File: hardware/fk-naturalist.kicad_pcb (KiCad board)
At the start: 2 copper layers, 28.7 x 87.4 mm, 132 parts, among them J1 CONN_01X06, J10 S2B-PH-SM4-TB, J11 RF-SMA-EDGE, J5 Conn_01x03, J6 Conn_01x05, J7 CONN-HDR-2x5, J8 Conn_01x09, J9 MICRO-USB, M1 MOUNT_HOLE, M3 MOUNT_HOLE, M4 MOUNT_HOLE, M6 MOUNT_HOLE, M7 MICROSD, Q1 2N7002LT1G, Q2 2N7002LT1G, Q3 2N7002LT1G, Q4 2N7002LT1G, SW1 SPNO, SW2 SPNO, U1 ATWINC1500-MR210PA, U10 FGPMMOPA6H, U101 TSL2591, U102 MPL3115A2, U103 BNO055, U104 SHT31, U11 MAX1704XX, U2 ATSAMD21G18A-AU, U3 SPH0645, U4 24AA02E64, U5 S25FL116K0XMFI041, U6 BQ24074RGTT, U7 PCF8523, U8 MCP1700T-3302E/MB, U9 ISL8541x, Y1 FC-135, Y101 FC-135, Y2 FC-135

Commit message: Working on the new PCB layout.
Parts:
- removed C2: 100nF, RocketScreamKicadLibrary:CAP-0603
- removed C23: 1uF 10V X5R, RocketScreamKicadLibrary:CAP-0603
- removed J1: CONN_01X06, Socket_Strips:Socket_Strip_Straight_1x06_Pitch2.54mm
- removed R101: 10K, Resistors_SMD:R_0603_HandSoldering
- removed U8: MCP1700T-3302E/MB, RocketScreamKicadLibrary:SOT-89
- BT1: footprint Connectors:CR1220 -> conservify:BAT_CR1210; moved to B.Cu
- C1: value 4.7uF 10V X5R -> 1uF
- C101, C102, C103, C104, C105, C106, C107, C108, C109, C13, C15, C22, C24: footprint Capacitors_SMD:C_0603_HandSoldering -> RocketScreamKicadLibrary:CAP-0603
- M7, U1, U10: moved to B.Cu
- R102, R103, R11, R12, R26, R27, R37: footprint Resistors_SMD:R_0603_HandSoldering -> RocketScreamKicadLibrary:RES-0603
- moved M3 125.3 mm to (79.3, 144.9)
- moved U9 109.7 mm to (102.8, 121.2), turned to 90 degrees
- moved R2 108.5 mm to (109.1, 144.8), turned to 270 degrees
- moved R31 108.4 mm to (79.9, 116.6), turned to 180 degrees
- moved R41 104.8 mm to (96.1, 134.8), turned to 180 degrees
- moved D2 103.3 mm to (95.1, 144.8), turned to 90 degrees
- moved C28 99.9 mm to (96.1, 133.0), turned to 180 degrees
- moved C12 99.4 mm to (93.9, 115.5), turned to 180 degrees
- moved U11 99.4 mm to (91.0, 135.3), turned to 180 degrees
- moved M7 99.1 mm to (93.4, 142.7), turned to 90 degrees
- moved J7 99.1 mm to (132.8, 138.6), turned to 270 degrees
- moved J8 99.0 mm to (134.3, 144.4), turned to 270 degrees
- moved R43 94.2 mm to (87.8, 133.9), turned to 90 degrees
- moved Y2 93.7 mm to (151.0, 142.5), turned to 90 degrees
- moved L2 93.4 mm to (89.9, 123.8), turned to 270 degrees
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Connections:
- C24 pad 1: Net-(C24-Pad1) -> 3V3
- J9 pad 6: Net-(J9-Pad6) -> Net-(C14-Pad1)
- J9 pad 7: Net-(C14-Pad1) -> Net-(J9-Pad7)
- R37 pad 1: Net-(C24-Pad1) -> 3V3
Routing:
- net 3V3: track 0.00 -> 292.7 mm, vias 0 -> 14
- net /SCL: track 0.00 -> 243.0 mm, vias 0 -> 11
- net /SDA: track 0.00 -> 241.1 mm, vias 0 -> 10
- net /SCK: track 0.00 -> 73.2 mm, vias 0 -> 3
- net /MOSI: track 0.00 -> 67.6 mm, vias 0 -> 3
- net /MISO: track 0.00 -> 65.9 mm, vias 0 -> 3
- net /I2S_BCLK: track 0.00 -> 57.3 mm, vias 0 -> 2
- net /USB-: track 0.00 -> 57.3 mm, vias 0 -> 2
- net /USB+: track 0.00 -> 55.5 mm, vias 0 -> 2
- net /SD_CS: track 0.00 -> 55.4 mm, vias 0 -> 3
- net /I2S_WS: track 0.00 -> 52.8 mm, vias 0 -> 2
- net /D13: track 0.00 -> 52.7 mm, vias 0 -> 3
- net VBAT: track 0.00 -> 51.5 mm, vias 0 -> 4
- net /I2S_DATA: track 0.00 -> 51.0 mm, vias 0 -> 2
- net /WIFI_RST: track 0.00 -> 48.2 mm, vias 0 -> 3
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- added copper zone on B.Cu, net GND
- added copper zone on F.Cu, net GND
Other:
- board size 28.7 x 87.4 mm -> 100 x 37 mm
- board text added: "A3"
- board text added: "A4"
- board text added: "A5"
- board text added: "D13"

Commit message: Everything is connected, time to cleanup.
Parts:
- moved R103 10.9 mm to (148.4, 133.5), turned to 270 degrees
- moved R35 8.43 mm to (165.0, 124.0), turned to 270 degrees
- moved R36 5.69 mm to (163.4, 124.0), turned to 270 degrees
- moved R45 4.93 mm to (98.1, 122.2), turned to 0 degrees
- moved C29 4.03 mm to (98.6, 127.1), turned to 270 degrees
- moved C10 3.77 mm to (88.5, 121.6), turned to 0 degrees
- moved F1 1.98 mm to (88.7, 125.3), turned to 180 degrees
- moved C108 1.79 mm to (152.5, 133.5), turned to 90 degrees
- moved L2 1.42 mm to (88.5, 123.3), turned to 0 degrees
- moved R102 1.24 mm to (150.7, 133.5), turned to 270 degrees
- moved C12 0.76 mm to (93.1, 115.5)
- moved C20 0.76 mm to (93.1, 118.9)
- moved C21 0.76 mm to (93.1, 120.5)
- moved R21 0.76 mm to (93.1, 117.2)
- moved R44 0.71 mm to (98.9, 119.6)
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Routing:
- net 3V3: track 292.7 -> 386.0 mm, vias 14 -> 28
- net Net-(J9-Pad4): track 1.63 -> 56.9 mm, vias 0 -> 2
- net GND: track 20.0 -> 52.6 mm, vias 1 -> 21
- net 5V0: track 1.73 -> 20.2 mm, vias 0 -> 2
- net Net-(C29-Pad1): track 3.23 -> 15.5 mm, vias 0 -> 3
- net Net-(J11-Pad1): track 0.00 -> 8.99 mm, vias 0 -> 1
- net Net-(C30-Pad1): track 1.13 -> 9.51 mm, vias 1 -> 0
- net /ISL_VIN: track 16.9 -> 24.6 mm
- net VBUS: track 41.2 -> 48.4 mm, vias 2 -> 3
- net Net-(R103-Pad1): track 0.00 -> 4.36 mm
- net /SCL: track 243.0 -> 247.0 mm, vias 11 -> 12
- net /SDA2: track 42.4 -> 46.2 mm
- net /CHG: track 12.8 -> 9.80 mm
- net /SDA: track 241.1 -> 243.5 mm, vias 10 -> 11
- net Net-(D9-Pad1): track 0.00 -> 1.96 mm
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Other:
- net class RF-50Ohm removed

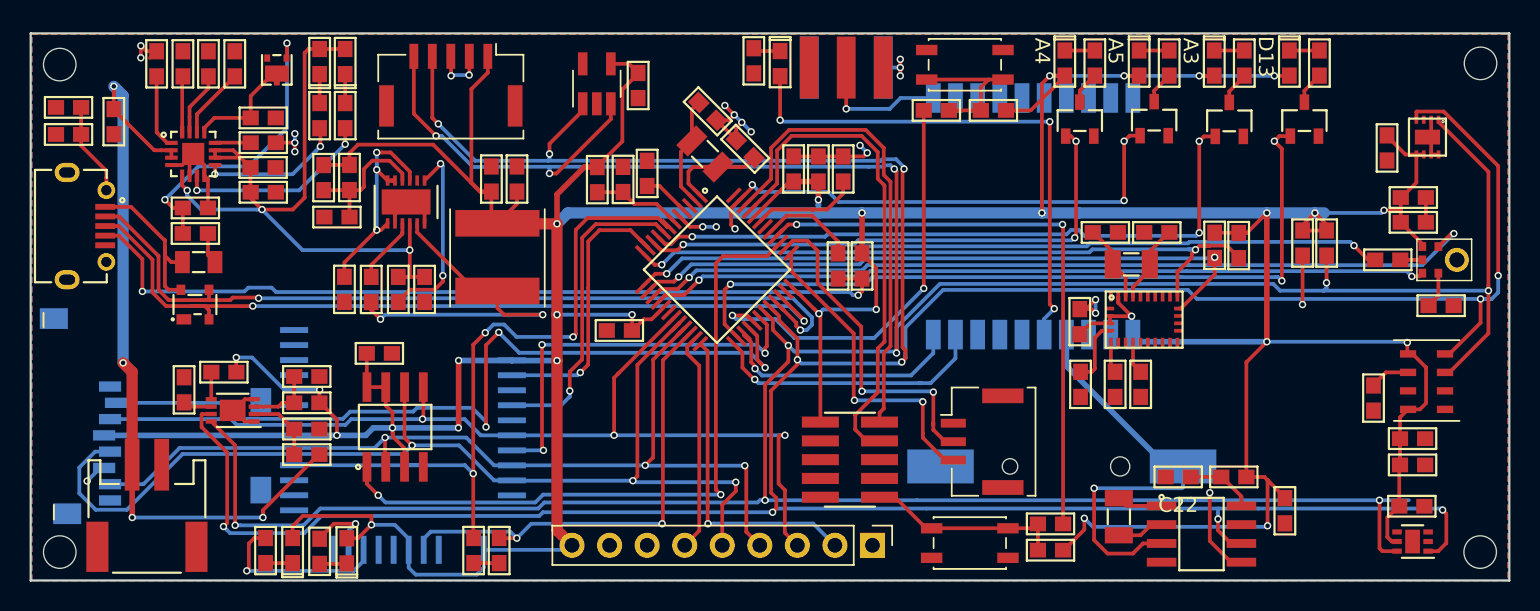
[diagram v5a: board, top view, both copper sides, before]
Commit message: Some power fills, cleaning up warnings.
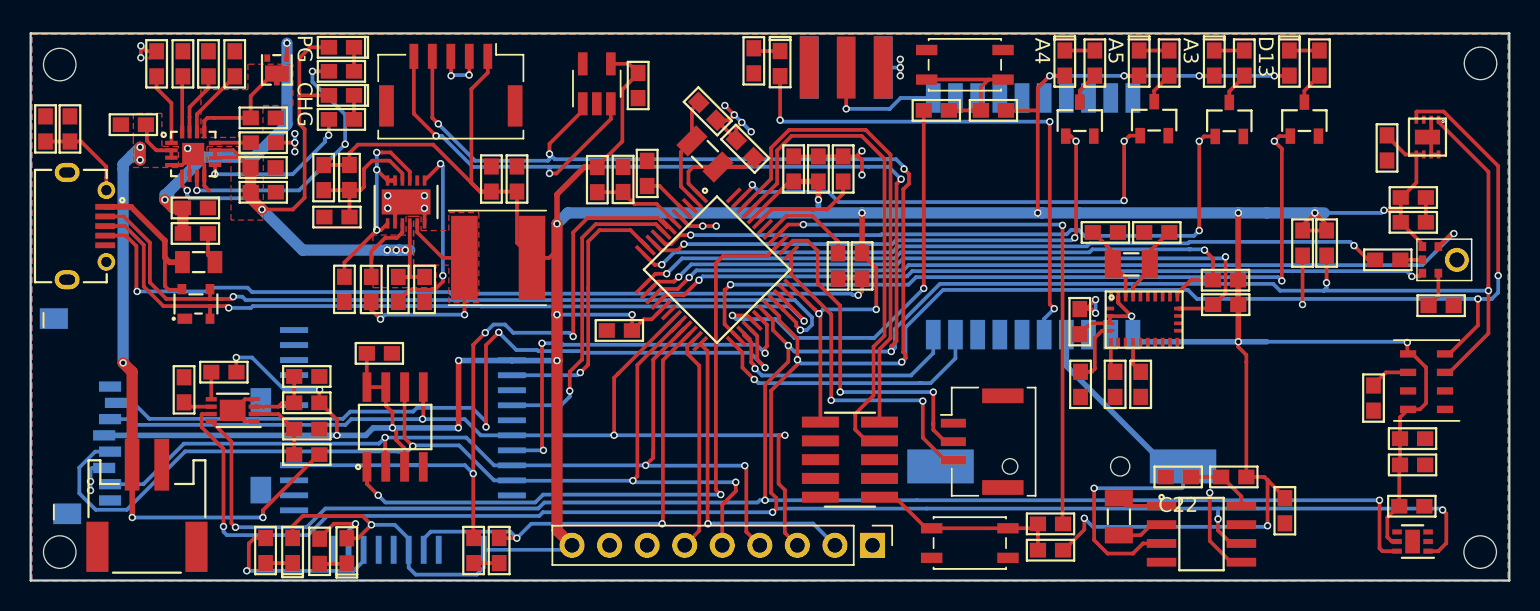
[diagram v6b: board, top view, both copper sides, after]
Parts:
- moved R27 4.08 mm to (158.2, 128.1), turned to 0 degrees
- moved R32 3.01 mm to (98.4, 112.4), turned to 0 degrees
- moved D10 2.72 mm to (98.4, 114.0), turned to 180 degrees
- moved R26 2.50 mm to (158.2, 126.5), turned to 0 degrees
- moved R31 1.60 mm to (78.4, 116.3), turned to 90 degrees
- moved R33 1.49 mm to (98.4, 115.6), turned to 0 degrees
- moved C14 1.46 mm to (80.0, 116.3), turned to 90 degrees
- moved C19 1.34 mm to (84.3, 116.0), turned to 180 degrees
- moved D9 1.00 mm to (98.4, 110.7), turned to 180 degrees
- moved D8 0.08 mm to (88.6, 128.1)
- turned L5 to 0 degrees
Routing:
- net /ISL_VIN: track 24.6 -> 15.6 mm
- net 3V3: track 386.0 -> 377.5 mm
- net /PG: track 13.4 -> 19.7 mm, vias 2 -> 3
- net VBAT: track 51.5 -> 45.3 mm, vias 4 -> 5
- net VBUS: track 48.4 -> 51.2 mm, vias 3 -> 5
- net /SCL2: track 43.9 -> 46.3 mm
- net /A5: track 34.6 -> 32.4 mm, vias 4 -> 3
- net /SDA: track 243.5 -> 241.5 mm
- net /SDA2: track 46.2 -> 44.4 mm
- net /D30: track 21.5 -> 22.5 mm
- net /D31: track 22.6 -> 23.5 mm
- net /CHG: track 9.80 -> 10.6 mm
- net /RESET: track 40.8 -> 40.0 mm
- net /SCL: track 247.0 -> 247.7 mm
- net VUSB: track 11.2 -> 10.6 mm
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- added copper zone on F.Cu, net /ISL_VIN
- added copper zone on F.Cu, net VBAT
- added copper zone on F.Cu, net VBUS
- added copper zone on F.Cu, net VEXT
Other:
- rule trace_min: 0.19 -> 0.1524
- board text added: "CHG"
- board text added: "PG"

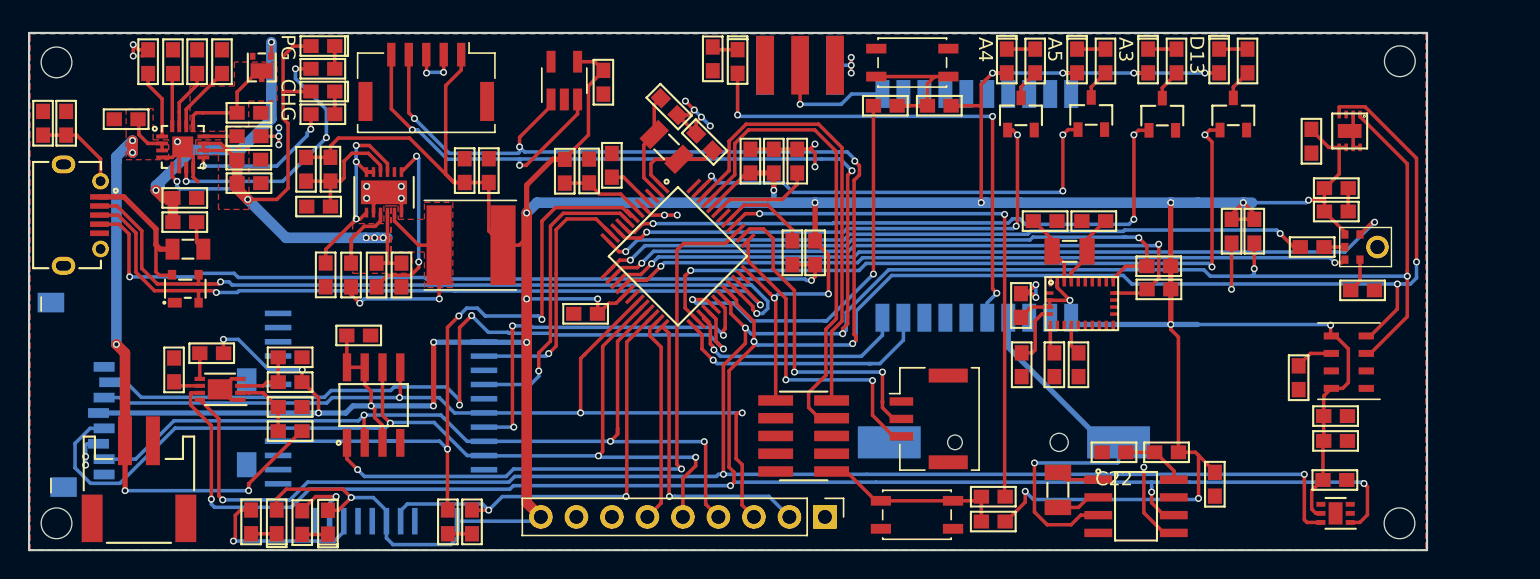
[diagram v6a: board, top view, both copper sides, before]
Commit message: Breakaway part for sensors.
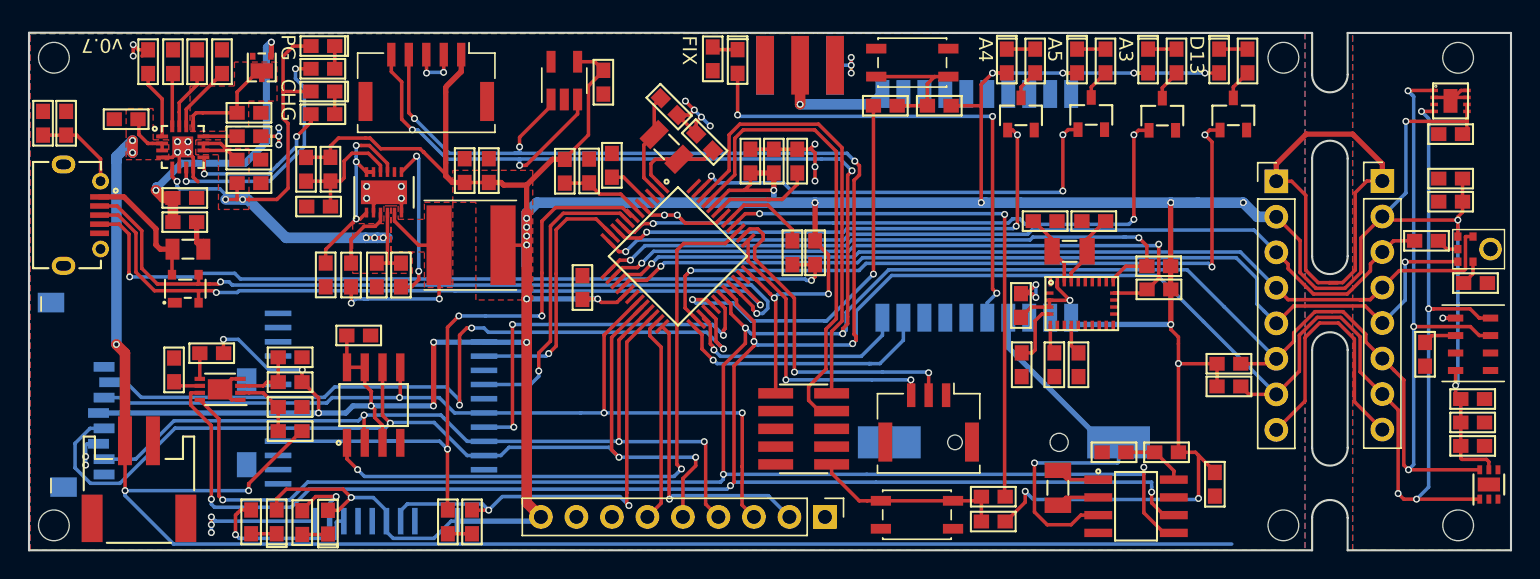
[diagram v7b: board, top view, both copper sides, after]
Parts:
- added G***: LOGO, conservify:conservify_text_negative_4000, B.Cu at (161.2, 128.6)
- added G***: LOGO, conservify:fk_negative_2500, B.Cu at (163.7, 129.0)
- added J1: Conn_01x08, Socket_Strips:Socket_Strip_Straight_1x08_Pitch2.54mm, F.Cu at (166.6, 120.4)
- added J2: Conn_01x08, Socket_Strips:Socket_Strip_Straight_1x08_Pitch2.54mm, F.Cu at (174.2, 120.4)
- added M1: MOUNT_HOLE, RocketScreamKicadLibrary:HOLE_NPTH_2.2MM, F.Cu at (167.1, 145.0)
- added M4: MOUNT_HOLE, RocketScreamKicadLibrary:HOLE_NPTH_2.2MM, F.Cu at (179.6, 111.6)
- moved U101 11.2 mm to (181.8, 142.1), turned to 90 degrees
- moved R36 11.1 mm to (163.2, 135.1), turned to 0 degrees
- moved C101 10.2 mm to (180.6, 139.3)
- moved C109 9.97 mm to (179.1, 117.0), turned to 180 degrees
- moved C104 9.89 mm to (180.6, 137.7)
- moved C103 9.88 mm to (180.6, 136.0)
- moved R35 9.65 mm to (163.2, 133.5), turned to 0 degrees
- moved C102 9.20 mm to (177.2, 132.8)
- moved U102 8.98 mm to (181.0, 132.1)
- moved C15 8.51 mm to (179.1, 120.2), turned to 180 degrees
- moved M4 8.33 mm to (167.1, 111.6)
- moved C13 8.24 mm to (179.1, 121.9), turned to 180 degrees
- moved R12 8.19 mm to (177.3, 124.7)
- moved R11 8.09 mm to (180.8, 127.7)
- moved U3 8.09 mm to (181.9, 125.3)
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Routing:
- net VBAT: track 45.3 -> 126.2 mm
- net GND: track 53.0 -> 98.3 mm, vias 27 -> 34
- net 3V3: track 377.5 -> 403.6 mm, vias 28 -> 34
- net Net-(J1-Pad8): track 0.00 -> 19.2 mm
- net /SDA: track 241.5 -> 259.6 mm
- net /I2S_WS: track 52.8 -> 68.3 mm
- net /SCL: track 247.7 -> 262.0 mm
- net /I2S_DATA: track 51.0 -> 62.6 mm, vias 2 -> 1
- net /I2S_BCLK: track 57.3 -> 66.9 mm, vias 2 -> 1
- net /PG: track 19.7 -> 17.8 mm, vias 3 -> 2
- net /D30: track 22.5 -> 21.1 mm
- net /MOSI: track 67.4 -> 66.0 mm
- net VUSB: track 10.6 -> 9.28 mm
- net Net-(R38-Pad1): track 13.2 -> 12.0 mm
- net /SWCLK: track 35.2 -> 34.0 mm
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- added copper zone on F.Cu, net 3V3
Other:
- board size 100 x 37 mm -> 106 x 37 mm
- board text added: "FIX"
- board text added: "v0.7"
